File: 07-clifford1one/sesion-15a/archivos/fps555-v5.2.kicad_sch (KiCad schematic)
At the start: 21 parts, among them M1 Motorreductor, U1 555, U2 L293D

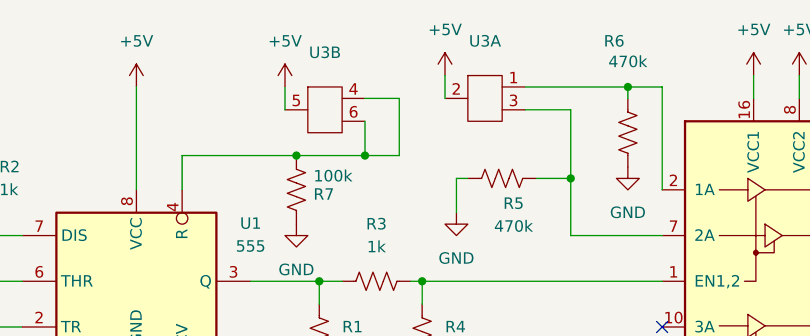
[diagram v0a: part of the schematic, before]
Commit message: cambios corresponidnetes al modo pcb de kicad
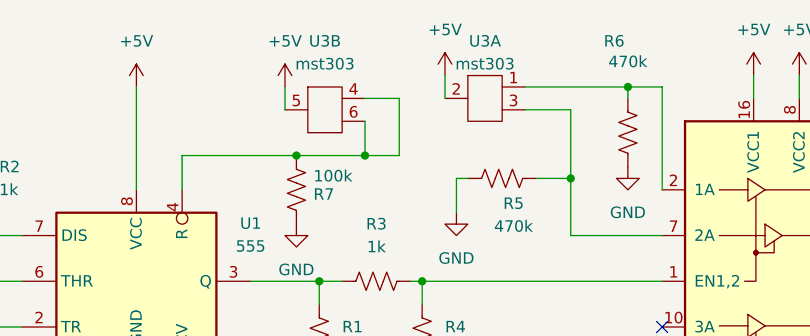
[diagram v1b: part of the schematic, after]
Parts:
- C1: footprint (none) -> Capacitor_THT:C_Disc_D5.0mm_W2.5mm_P2.50mm
- C2: footprint (none) -> Capacitor_THT:C_Disc_D5.1mm_W3.2mm_P5.00mm
- D1: footprint (none) -> LED_THT:LED_D3.0mm_Clear
- M1: footprint (none) -> Connector_PinHeader_1.00mm:PinHeader_1x02_P1.00mm_Vertical
- R1, R2, R3, R4, R5, R6, R7: footprint (none) -> Resistor_THT:R_Axial_DIN0207_L6.3mm_D2.5mm_P7.62mm_Horizontal
- RV1: footprint (none) -> Potentiometer_THT:Potentiometer_Vishay_148-149_Single_Horizontal
- U3: value ~ -> mst303; footprint (none) -> Connector_PinHeader_1.00mm:PinHeader_1x02_P1.00mm_Vertical
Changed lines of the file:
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@@
 			)
 		)
-		(property "Footprint" ""
+		(property "Footprint" "Resistor_THT:R_Axial_DIN0207_L6.3mm_D2.5mm_P7.62mm_Horizontal"
 			(at 94.996 68.834 90)
 			(effects
@@
 			)
 		)
-		(property "Footprint" ""
+		(property "Footprint" "Capacitor_THT:C_Disc_D5.1mm_W3.2mm_P5.00mm"
 			(at 56.8452 82.55 0)
 			(effects
@@
 			)
 		)
-		(property "Value" "~"
+		(property "Value" "mst303"
 			(at 112.395 38.1 0)
 			(effects
@@
 			)
 		)
-		(property "Footprint" ""
+		(property "Footprint" "Connector_PinHeader_1.00mm:PinHeader_1x02_P1.00mm_Vertical"
 			(at 111.76 40.64 0)
 			(effects
@@
 			)
 		)
-		(property "Footprint" ""
+		(property "Footprint" "LED_THT:LED_D3.0mm_Clear"
 			(at 93.98 78.74 0)
 			(effects
@@
 			)
 		)
-		(property "Footprint" ""
+		(property "Footprint" "Capacitor_THT:C_Disc_D5.0mm_W2.5mm_P2.50mm"
 			(at 79.7052 82.55 0)
 			(effects
@@
 			)
 		)
-		(property "Footprint" ""
+		(property "Footprint" "Resistor_THT:R_Axial_DIN0207_L6.3mm_D2.5mm_P7.62mm_Horizontal"
 			(at 106.426 68.834 90)
 			(effects
@@
 			)
 		)
-		(property "Footprint" ""
+		(property "Footprint" "Resistor_THT:R_Axial_DIN0207_L6.3mm_D2.5mm_P7.62mm_Horizontal"
 			(at 56.896 51.054 90)
 			(effects
@@
 			)
 		)
-		(property "Footprint" ""
+		(property "Footprint" "Potentiometer_THT:Potentiometer_Vishay_148-149_Single_Horizontal"
 			(at 31.75 68.58 0)
 			(effects
@@
 			)
 		)
-		(property "Footprint" ""
+		(property "Footprint" "Resistor_THT:R_Axial_DIN0207_L6.3mm_D2.5mm_P7.62mm_Horizontal"
 			(at 100.584 61.214 90)
 			(effects
@@
 			)
 		)
-		(property "Footprint" ""
+		(property "Footprint" "Resistor_THT:R_Axial_DIN0207_L6.3mm_D2.5mm_P7.62mm_Horizontal"
 			(at 127.254 45.466 90)
 			(effects
@@
 			)
 		)
-		(property "Footprint" ""
+		(property "Footprint" "Connector_PinHeader_1.00mm:PinHeader_1x02_P1.00mm_Vertical"
 			(at 177.8 61.976 0)
 			(effects
@@
 		(fields_autoplaced yes)
 		(property "Reference" "U3"
-			(at 94.615 36.83 0)
-			(effects
-				(font
-					(size 1.27 1.27)
-				)
-			)
-		)
-		(property "Value" "~"
-			(at 94.615 39.37 0)
-			(effects
-				(font
-					(size 1.27 1.27)
-				)
-			)
-		)
-		(property "Footprint" ""
+			(at 94.615 35.56 0)
+			(effects
+				(font
+					(size 1.27 1.27)
+				)
+			)
+		)
+		(property "Value" "mst303"
+			(at 94.615 38.1 0)
+			(effects
+				(font
+					(size 1.27 1.27)
+				)
+			)
+		)
+		(property "Footprint" "Connector_PinHeader_1.00mm:PinHeader_1x02_P1.00mm_Vertical"
 			(at 93.98 41.91 0)
 			(effects
@@
 			)
 		)
-		(property "Footprint" ""
+		(property "Footprint" "Resistor_THT:R_Axial_DIN0207_L6.3mm_D2.5mm_P7.62mm_Horizontal"
 			(at 114.554 49.784 90)
 			(effects
@@
 			)
 		)
-		(property "Footprint" ""
+		(property "Footprint" "Resistor_THT:R_Axial_DIN0207_L6.3mm_D2.5mm_P7.62mm_Horizontal"
 			(at 90.424 51.816 90)
 			(effects

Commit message: cambios kicad
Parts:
- added D8: 4007, Diode_THT:D_A-405_P10.16mm_Horizontal, symbol Diode:1N4148WT
- added J1: Screw_Terminal_01x02, TerminalBlock:TerminalBlock_MaiXu_MX126-5.0-02P_1x02_P5.00mm, symbol Connector:Screw_Terminal_01x02
- D2, D3: value 1n4148 -> 4007; footprint Diode_SMD:D_SOD-523 -> Diode_THT:D_A-405_P10.16mm_Horizontal
- D4, D5, D6, D7: footprint Diode_SMD:D_SOD-523 -> Diode_THT:D_A-405_P10.16mm_Horizontal
- M1: footprint Connector_PinHeader_1.00mm:PinHeader_1x02_P1.00mm_Vertical -> TerminalBlock:TerminalBlock_MaiXu_MX126-5.0-02P_1x02_P5.00mm
- R1, R3, R4, R5, R6, R7: footprint Resistor_THT:R_Axial_DIN0207_L6.3mm_D2.5mm_P7.62mm_Horizontal -> Resistor_THT:R_Axial_DIN0207_L6.3mm_D2.5mm_P10.16mm_Horizontal
- R2: value 1k -> 10k; footprint Resistor_THT:R_Axial_DIN0207_L6.3mm_D2.5mm_P7.62mm_Horizontal -> Resistor_THT:R_Axial_DIN0207_L6.3mm_D2.5mm_P10.16mm_Horizontal
- RV1: value 100k -> 500k; footprint Potentiometer_THT:Potentiometer_Vishay_148-149_Single_Horizontal -> Potentiometer_THT:Potentiometer_Omeg_PC16BU_Vertical
- U3: footprint Connector_PinHeader_1.00mm:PinHeader_1x02_P1.00mm_Vertical -> Connector_PinHeader_1.00mm:PinHeader_1x05_P1.00mm_Vertical
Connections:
- net GND: now also J1.1 (Pin_1)
- new net +9V: D8.2 (A), J1.2 (Pin_2)
- new net VCC: D8.1 (K)

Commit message: cambios kicad
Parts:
- J1: value Screw_Terminal_01x02 -> Batería 9v
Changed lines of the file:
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@@
 			)
 		)
-		(property "Value" "Screw_Terminal_01x02"
+		(property "Value" "Batería 9v"
 			(at 26.67 25.4 0)
 			(effects

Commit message: CAMBIOS KICAD
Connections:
- net +5V is gone; now on net VCC: D5.1 (K), D7.1 (K), R2.1, U1.8 (VCC), U2.16 (VCC1), U2.8 (VCC2), U3.2, U3.5
